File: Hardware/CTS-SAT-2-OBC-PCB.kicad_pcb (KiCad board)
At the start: 6 copper layers, 0 parts

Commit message: Prepare for layout
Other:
- board outline added: 100 x 100 mm
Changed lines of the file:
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@@
 	)
 	(net 0 "")
+	(gr_rect
+		(start 100 50)
+		(end 200 150)
+		(stroke
+			(width 0.05)
+			(type solid)
+		)
+		(fill no)
+		(layer "Edge.Cuts")
+	)
 	(embedded_fonts no)
 )

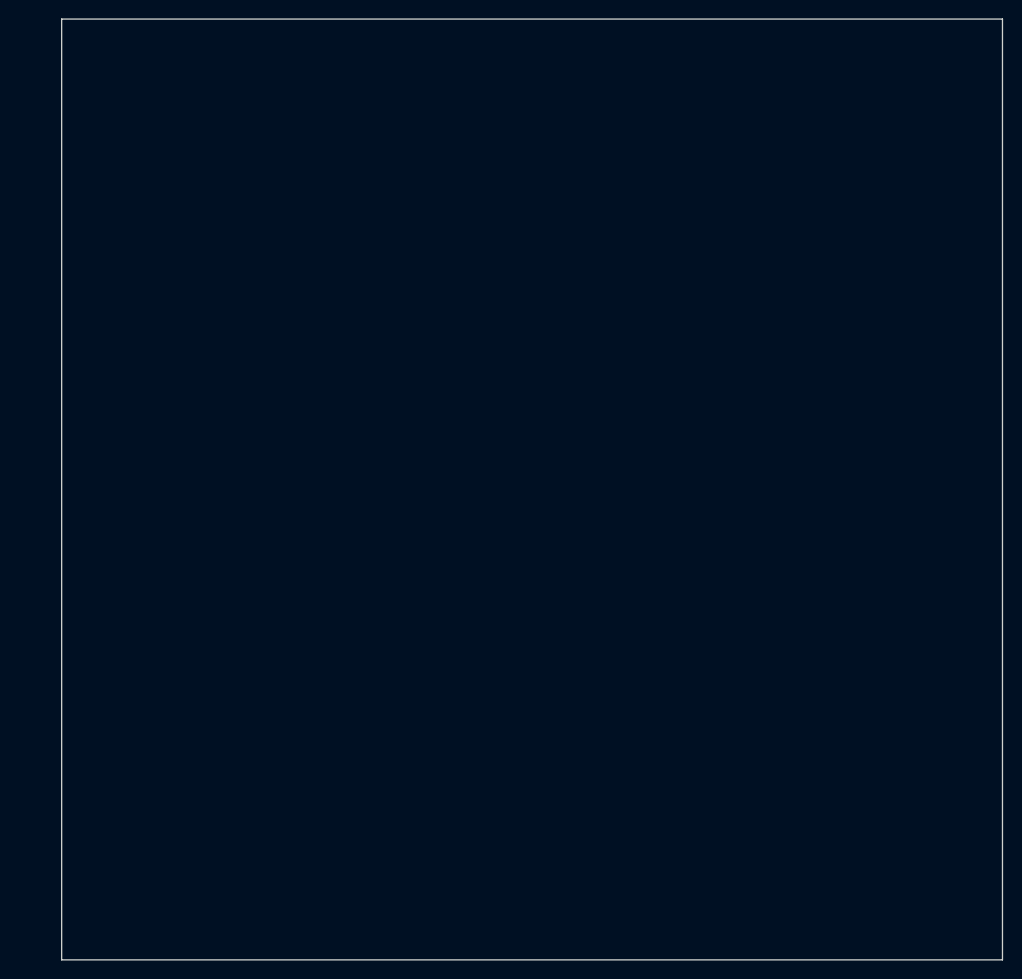
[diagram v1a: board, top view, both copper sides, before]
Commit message: Assign footprints
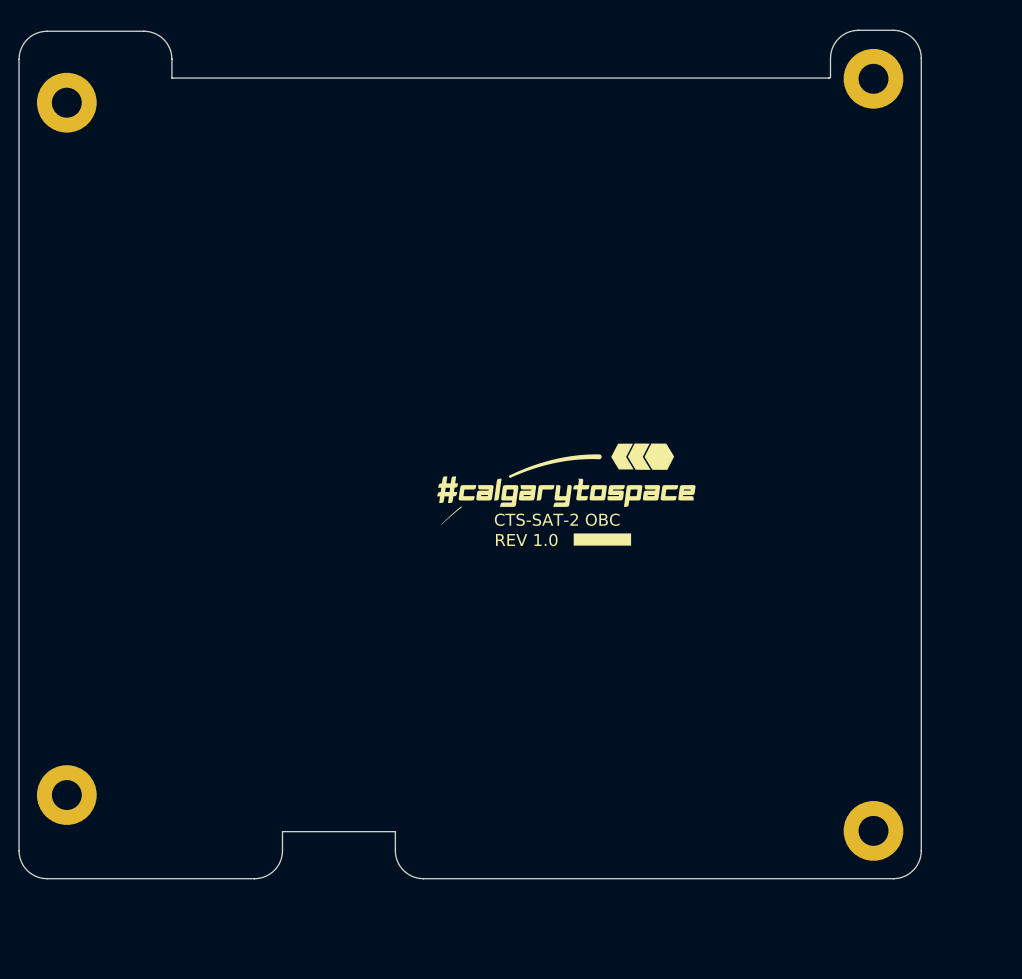
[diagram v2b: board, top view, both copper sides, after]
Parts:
- added *1: PC104 Mounting, OBC Development Board:PC104 MOUNTING POINTS, F.Cu at (102.3, 60.1)
- added *2: PC104 Mounting, OBC Development Board:PC104 MOUNTING POINTS, F.Cu at (186.3, 56.4)
- added *3: PC104 Mounting, OBC Development Board:PC104 MOUNTING POINTS, F.Cu at (102.3, 134.0)
- added *4: PC104 Mounting, OBC Development Board:PC104 MOUNTING POINTS, F.Cu at (184.4, 134.8)
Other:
- board size 100 x 100 mm -> 95.9 x 90.2 mm
- board text added: "CTS-SAT-2 OBC"
- board text added: "REV 1.0"

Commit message: Basic board shape
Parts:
- added C1: 15p, Capacitor_SMD:C_0402_1005Metric, F.Cu at (-55.8, 55.2)
- added C10: 100n, Capacitor_SMD:C_0402_1005Metric, F.Cu at (-52.9, 63.1)
- added C11: 100n, Capacitor_SMD:C_0402_1005Metric, F.Cu at (-50.0, 55.2)
- added C12: 100n, Capacitor_SMD:C_0402_1005Metric, F.Cu at (-50.0, 57.2)
- added C13: 100n, Capacitor_SMD:C_0402_1005Metric, F.Cu at (-50.0, 59.1)
- added C14: 100n, Capacitor_SMD:C_0402_1005Metric, F.Cu at (-50.0, 61.1)
- added C15: 100n, Capacitor_SMD:C_0402_1005Metric, F.Cu at (-81.8, 61.5)
- added C16: 1u, Capacitor_SMD:C_0402_1005Metric, F.Cu at (-81.8, 63.4)
- added C17: 100n, Capacitor_SMD:C_0402_1005Metric, F.Cu at (-81.8, 65.4)
- added C18: 100n, Capacitor_SMD:C_0402_1005Metric, F.Cu at (-81.8, 67.4)
- added C19: 100n, Capacitor_SMD:C_0402_1005Metric, F.Cu at (-81.8, 69.3)
- added C2: 15p, Capacitor_SMD:C_0402_1005Metric, F.Cu at (-55.8, 57.2)
- added C20: 4.7u, Capacitor_SMD:C_0402_1005Metric, F.Cu at (-81.8, 71.3)
- added C21: 100n, Capacitor_SMD:C_0402_1005Metric, F.Cu at (-81.8, 73.3)
- added C22: 100n, Capacitor_SMD:C_0402_1005Metric, F.Cu at (-79.0, 61.5)
- added C23: 100n, Capacitor_SMD:C_0603_1608Metric, F.Cu at (-81.3, 39.1)
- added C24: 100n, Capacitor_SMD:C_0402_1005Metric, F.Cu at (-79.0, 63.4)
- added C25: 100n, Capacitor_SMD:C_0402_1005Metric, F.Cu at (-79.0, 65.4)
- added C26: 100n, Capacitor_SMD:C_0603_1608Metric, F.Cu at (-81.3, 41.6)
- added C27: 100n, Capacitor_SMD:C_0402_1005Metric, F.Cu at (-79.0, 67.4)
- added C28: 100n, Capacitor_SMD:C_0402_1005Metric, F.Cu at (-79.0, 69.3)
- added C29: 15p, Capacitor_SMD:C_0603_1608Metric, F.Cu at (-81.3, 44.1)
- added C3: 100n, Capacitor_SMD:C_0402_1005Metric, F.Cu at (-55.8, 59.1)
- added C30: 100n, Capacitor_SMD:C_0402_1005Metric, F.Cu at (-79.0, 71.3)
- added C31: 100n, Capacitor_SMD:C_0402_1005Metric, F.Cu at (-79.0, 73.3)
- added C32: 100n, Capacitor_SMD:C_0402_1005Metric, F.Cu at (-76.1, 61.5)
- added C33: 100n, Capacitor_SMD:C_0402_1005Metric, F.Cu at (-76.1, 63.4)
- added C34: 100n, Capacitor_SMD:C_0402_1005Metric, F.Cu at (-76.1, 65.4)
- added C35: 100n, Capacitor_SMD:C_0402_1005Metric, F.Cu at (-76.1, 67.4)
- added C36: 4.7uF, Capacitor_SMD:C_1206_3216Metric, F.Cu at (-48.7, 23.4)
- added C37: 4.7uF, Capacitor_SMD:C_1206_3216Metric, F.Cu at (-48.7, 26.8)
- added C38: 4.7uF, Capacitor_SMD:C_1206_3216Metric, F.Cu at (-48.7, 30.1)
- added C39: 0.1u, Capacitor_SMD:C_0603_1608Metric, F.Cu at (-22.0, -14.0)
- added C4: 100n, Capacitor_SMD:C_0402_1005Metric, F.Cu at (-55.8, 61.1)
- added C40: 0.1u, Capacitor_SMD:C_0603_1608Metric, F.Cu at (-22.0, -11.5)
- added C41: 0.1u, Capacitor_SMD:C_0603_1608Metric, F.Cu at (-22.0, -9.01)
- added C42: 0.1u, Capacitor_SMD:C_0603_1608Metric, F.Cu at (-22.0, -6.50)
- added C43: 100pF, Capacitor_SMD:C_0603_1608Metric, F.Cu at (-25.3, 68.1)
- added C44: 100pF, Capacitor_SMD:C_0603_1608Metric, F.Cu at (-25.3, 70.7)
- added C45: 33 pF, Capacitor_SMD:C_0603_1608Metric, F.Cu at (-25.3, 73.2)
- added C46: 33 pF, Capacitor_SMD:C_0603_1608Metric, F.Cu at (-25.3, 75.7)
- added C47: 100pF, Capacitor_SMD:C_0603_1608Metric, F.Cu at (-25.3, 78.2)
- added C48: 0.1uF, Capacitor_SMD:C_0603_1608Metric, F.Cu at (-25.3, 80.7)
- added C49: 0.1uF, Capacitor_SMD:C_0603_1608Metric, F.Cu at (-33.9, 43.5)
- added C5: 100n, Capacitor_SMD:C_0402_1005Metric, F.Cu at (-55.8, 63.1)
- added C50: 1uF, Capacitor_SMD:C_0603_1608Metric, F.Cu at (-33.9, 46.0)
- added C51: 0.1uF, Capacitor_SMD:C_0603_1608Metric, F.Cu at (-33.9, 48.5)
- added C52: 0.1uF, Capacitor_SMD:C_0603_1608Metric, F.Cu at (-33.9, 51.0)
- added C6: 1u, Capacitor_SMD:C_0402_1005Metric, F.Cu at (-52.9, 55.2)
- added C7: 100n, Capacitor_SMD:C_0402_1005Metric, F.Cu at (-52.9, 57.2)
- added C8: 1u, Capacitor_SMD:C_0402_1005Metric, F.Cu at (-52.9, 59.1)
- added C9: 100n, Capacitor_SMD:C_0402_1005Metric, F.Cu at (-52.9, 61.1)
- added D1: LED, CTS-SAT-1:D-SML-D12U1WT86, F.Cu at (-65.9, 68.5)
- added D2: LED, CTS-SAT-1:D-SML-D12U1WT86, F.Cu at (-65.9, 70.6)
- added D3: LED, CTS-SAT-1:D-SML-D12U1WT86, F.Cu at (-65.9, 72.6)
- added D4: LED, CTS-SAT-1:D-SML-D12U1WT86, F.Cu at (-44.1, 22.7)
- added D5: LED, CTS-SAT-1:D-SML-D12U1WT86, F.Cu at (-44.1, 24.8)
- added D6: LED, CTS-SAT-1:D-SML-D12U1WT86, F.Cu at (-44.1, 26.8)
- added IC1: STTS22HTR, STTS22HTR:SON65P200X200X55-7N-D, F.Cu at (-105.5, 68.1)
- added IC2: MT29F1G01ABAFDSF-AAT_F_TR, Package_SO:SOIC-16W_7.5x10.3mm_P1.27mm, F.Cu at (-30.5, -9.24)
- added IC3: MT29F1G01ABAFDSF-AAT_F_TR, Package_SO:SOIC-16W_7.5x10.3mm_P1.27mm, F.Cu at (-30.5, 2.72)
- added IC4: MT29F1G01ABAFDSF-AAT_F_TR, Package_SO:SOIC-16W_7.5x10.3mm_P1.27mm, F.Cu at (-30.5, 14.7)
- added IC5: MT29F1G01ABAFDSF-AAT_F_TR, Package_SO:SOIC-16W_7.5x10.3mm_P1.27mm, F.Cu at (-30.5, 26.6)
- added J10: J-0532610871, CTS-SAT-1:J-532610871, F.Cu at (-72.5, 20.1)
- added J11: J-TSW-106-05-T-S, CTS-SAT-1:J-TSW-106-05-T-S, F.Cu at (-78.4, 0.32)
- added J12: J-0532610671, CTS-SAT-1:J-0532610671, F.Cu at (-88.4, 11.2)
- added J13: J-0532610471, CTS-SAT-1:J-53261-0471, F.Cu at (-101.6, 7.42)
- added J14: J-0532610471, CTS-SAT-1:J-53261-0471, F.Cu at (-101.6, 15.1)
- added J15: J-TSW-106-05-T-S, CTS-SAT-1:J-TSW-106-05-T-S, F.Cu at (-78.4, 4.79)
- added J16: J-0532610671, CTS-SAT-1:J-0532610671, F.Cu at (-88.4, 19.5)
- added J17: J-0532610471, CTS-SAT-1:J-53261-0471, F.Cu at (-101.6, 22.7)
- added J18: 252105, CTS-SAT-1:J-252105, F.Cu at (-31.6, 71.2)
- added J19: 252105, CTS-SAT-1:J-252105, F.Cu at (-31.6, 79.8)
- added J2: 2-Pin Header, Connector_PinHeader_1.27mm:PinHeader_1x02_P1.27mm_Vertical, F.Cu at (-61.9, 23.4)
- added J20: 252105, CTS-SAT-1:J-252105, F.Cu at (-31.6, 88.5)
- added J21: J-0530471010, CTS-SAT-1:J-0530471010, F.Cu at (-9.95, 68.6)
- added J22: J-0530471010, CTS-SAT-1:J-0530471010, F.Cu at (-22.6, 39.6)
- added J23: J-0532610471, CTS-SAT-1:J-53261-0471, F.Cu at (-29.9, 59.3)
- added J24: USB_C_Receptacle_USB2.0_14P, Connector_USB:USB_C_Receptacle_JAE_DX07S024WJ3R400, F.Cu at (-50.2, 41.4)
- added J25: J-0532610471, CTS-SAT-1:J-53261-0471, F.Cu at (-101.6, 30.3)
- added J3: ESQ-126-14-G-D, ESQ-126-14-G-D:SAMTEC_ESQ-126-14-G-D, B.Cu at (112.7, 126.2)
- added J4: ESQ-126-14-G-D, ESQ-126-14-G-D:SAMTEC_ESQ-126-14-G-D, B.Cu at (107.6, 126.2)
- added J5: 2-Pin Header, Connector_PinHeader_1.27mm:PinHeader_1x02_P1.27mm_Vertical, F.Cu at (-57.7, 23.4)
- added J6: 2-Pin Header, Connector_PinHeader_1.27mm:PinHeader_1x02_P1.27mm_Vertical, F.Cu at (-53.6, 23.4)
- added J7: J-0532610671, CTS-SAT-1:J-0532610671, F.Cu at (-88.4, 2.88)
- added J8: J-0532610471, CTS-SAT-1:J-53261-0471, F.Cu at (-101.6, -0.21)
- added J9: J-0532610871, CTS-SAT-1:J-532610871, F.Cu at (-72.5, 11.8)
- added R1: 10k (NP), Resistor_SMD:R_0402_1005Metric, F.Cu at (-59.8, 56.4)
- added R10: 4k7, Resistor_SMD:R_0603_1608Metric, F.Cu at (-59.2, 49.2)
- added R100: 22R, Resistor_SMD:R_0603_1608Metric, F.Cu at (-65.2, 54.2)
- added R101: 22R, Resistor_SMD:R_0603_1608Metric, F.Cu at (-65.2, 56.7)
- added R102: 5k1, Resistor_SMD:R_0603_1608Metric, F.Cu at (-59.2, 51.7)
- added R103: 5k1, Resistor_SMD:R_0603_1608Metric, F.Cu at (-59.2, 54.2)
- added R11: 4k7, Resistor_SMD:R_0603_1608Metric, F.Cu at (-81.3, 46.7)
- added R12: 4k7, Resistor_SMD:R_0603_1608Metric, F.Cu at (-81.3, 49.2)
- added R13: 22R, Resistor_SMD:R_0603_1608Metric, F.Cu at (-81.3, 51.7)
- added R14: 22R, Resistor_SMD:R_0603_1608Metric, F.Cu at (-81.3, 54.2)
- added R15: 0R, Resistor_SMD:R_0603_1608Metric, F.Cu at (-81.3, 56.7)
- added R16: 22R, Resistor_SMD:R_0603_1608Metric, F.Cu at (-81.3, 59.2)
- added R17: 22R, Resistor_SMD:R_0603_1608Metric, F.Cu at (-77.2, 39.1)
- added R18: 0R, Resistor_SMD:R_0603_1608Metric, F.Cu at (-77.2, 41.6)
- added R19: 22R, Resistor_SMD:R_0603_1608Metric, F.Cu at (-77.2, 44.1)
- added R2: 1k, Resistor_SMD:R_0402_1005Metric, F.Cu at (-59.8, 58.4)
- added R20: 22R, Resistor_SMD:R_0603_1608Metric, F.Cu at (-77.2, 46.7)
- added R21: 22R, Resistor_SMD:R_0603_1608Metric, F.Cu at (-77.2, 49.2)
- added R22: 22R, Resistor_SMD:R_0603_1608Metric, F.Cu at (-77.2, 51.7)
- added R23: 22R, Resistor_SMD:R_0603_1608Metric, F.Cu at (-77.2, 54.2)
- added R24: 22R, Resistor_SMD:R_0603_1608Metric, F.Cu at (-77.2, 56.7)
- added R25: 22R, Resistor_SMD:R_0603_1608Metric, F.Cu at (-77.2, 59.2)
- added R26: 22R, Resistor_SMD:R_0603_1608Metric, F.Cu at (-73.2, 39.1)
- added R27: 0R, Resistor_SMD:R_0603_1608Metric, F.Cu at (-73.2, 41.6)
- added R28: 22R, Resistor_SMD:R_0603_1608Metric, F.Cu at (-73.2, 44.1)
- added R29: 22R, Resistor_SMD:R_0603_1608Metric, F.Cu at (-73.2, 46.7)
- added R3: 1k, Resistor_SMD:R_0402_1005Metric, F.Cu at (-59.8, 60.4)
- added R30: 22R, Resistor_SMD:R_0603_1608Metric, F.Cu at (-73.2, 49.2)
- added R31: 22R, Resistor_SMD:R_0603_1608Metric, F.Cu at (-73.2, 51.7)
- added R32: 22R, Resistor_SMD:R_0603_1608Metric, F.Cu at (-73.2, 54.2)
- added R33: 0R, Resistor_SMD:R_0603_1608Metric, F.Cu at (-73.2, 56.7)
- added R34: 0R, Resistor_SMD:R_0603_1608Metric, F.Cu at (-73.2, 59.2)
- added R35: 22R, Resistor_SMD:R_0603_1608Metric, F.Cu at (-69.2, 39.1)
- added R36: 22R, Resistor_SMD:R_0603_1608Metric, F.Cu at (-69.2, 41.6)
- added R37: 22R, Resistor_SMD:R_0603_1608Metric, F.Cu at (-69.2, 44.1)
- added R38: 22R, Resistor_SMD:R_0603_1608Metric, F.Cu at (-69.2, 46.7)
- added R39: 22R, Resistor_SMD:R_0603_1608Metric, F.Cu at (-69.2, 49.2)
- added R4: 0R, Resistor_SMD:R_0603_1608Metric, F.Cu at (-59.2, 39.1)
- added R40: 0R, Resistor_SMD:R_0603_1608Metric, F.Cu at (-69.2, 51.7)
- added R41: 22R, Resistor_SMD:R_0603_1608Metric, F.Cu at (-69.2, 54.2)
- added R42: 4k7, Resistor_SMD:R_0603_1608Metric, F.Cu at (-69.2, 56.7)
- added R43: 4k7, Resistor_SMD:R_0603_1608Metric, F.Cu at (-69.2, 59.2)
- added R44: 4k7, Resistor_SMD:R_0603_1608Metric, F.Cu at (-65.2, 39.1)
- added R45: 4k7, Resistor_SMD:R_0603_1608Metric, F.Cu at (-65.2, 41.6)
- added R46: 4k7, Resistor_SMD:R_0603_1608Metric, F.Cu at (-65.2, 44.1)
- added R47: 4k7, Resistor_SMD:R_0603_1608Metric, F.Cu at (-65.2, 46.7)
- added R48: 1k, Resistor_SMD:R_0603_1608Metric, F.Cu at (-65.2, 49.2)
- added R49: 1k, Resistor_SMD:R_0603_1608Metric, F.Cu at (-65.2, 51.7)
- added R5: 4k7, Resistor_SMD:R_0603_1608Metric, F.Cu at (-59.2, 41.6)
- added R50: 10K, Resistor_SMD:R_0603_1608Metric, F.Cu at (-62.0, 7.92)
- added R51: 10K, Resistor_SMD:R_0603_1608Metric, F.Cu at (-62.0, 10.4)
- added R52: 220R, Resistor_SMD:R_0603_1608Metric, F.Cu at (-62.0, 12.9)
- added R53: 220R, Resistor_SMD:R_0603_1608Metric, F.Cu at (-62.0, 15.4)
- added R54: 10k, Resistor_SMD:R_0603_1608Metric, F.Cu at (-62.0, 18.0)
- added R55: 0R, Resistor_SMD:R_0603_1608Metric, F.Cu at (-62.0, 20.5)
- added R56: 0R, Resistor_SMD:R_0603_1608Metric, F.Cu at (-58.0, 7.92)
- added R57: 0R, Resistor_SMD:R_0603_1608Metric, F.Cu at (-58.0, 10.4)
- added R58: 0R, Resistor_SMD:R_0603_1608Metric, F.Cu at (-58.0, 12.9)
- added R59: 0R, Resistor_SMD:R_0603_1608Metric, F.Cu at (-58.0, 15.4)
- added R6: 27.4, Resistor_SMD:R_0402_1005Metric, F.Cu at (-59.8, 62.4)
- added R60: 4K7, Resistor_SMD:R_0603_1608Metric, F.Cu at (-58.0, 18.0)
- added R61: 22R, Resistor_SMD:R_0603_1608Metric, F.Cu at (-58.0, 20.5)
- added R62: 0R, Resistor_SMD:R_0603_1608Metric, F.Cu at (-53.9, 7.92)
- added R63: 0R, Resistor_SMD:R_0603_1608Metric, F.Cu at (-53.9, 10.4)
- added R64: 0R, Resistor_SMD:R_0603_1608Metric, F.Cu at (-53.9, 12.9)
- added R65: 0R, Resistor_SMD:R_0603_1608Metric, F.Cu at (-53.9, 15.4)
- added R66: 0R, Resistor_SMD:R_0603_1608Metric, F.Cu at (-53.9, 18.0)
- added R67: 4K7, Resistor_SMD:R_0603_1608Metric, F.Cu at (-53.9, 20.5)
- added R68: 0R, Resistor_SMD:R_0603_1608Metric, F.Cu at (-49.9, 7.92)
- added R69: 0R, Resistor_SMD:R_0603_1608Metric, F.Cu at (-49.9, 10.4)
- added R7: 27.4, Resistor_SMD:R_0402_1005Metric, F.Cu at (-59.8, 64.4)
- added R70: 0R, Resistor_SMD:R_0603_1608Metric, F.Cu at (-49.9, 12.9)
- added R71: 4K7, Resistor_SMD:R_0603_1608Metric, F.Cu at (-49.9, 15.4)
- added R72: 10k, Resistor_SMD:R_0603_1608Metric, F.Cu at (-22.0, -3.99)
- added R73: 10k, Resistor_SMD:R_0603_1608Metric, F.Cu at (-22.0, -1.48)
- added R74: 10k, Resistor_SMD:R_0603_1608Metric, F.Cu at (-18.0, -14.0)
- added R75: 10k, Resistor_SMD:R_0603_1608Metric, F.Cu at (-18.0, -11.5)
- added R76: 22R, Resistor_SMD:R_0603_1608Metric, F.Cu at (-18.0, -9.01)
- added R77: 22R, Resistor_SMD:R_0603_1608Metric, F.Cu at (-18.0, -6.50)
- added R78: 22R, Resistor_SMD:R_0603_1608Metric, F.Cu at (-18.0, -3.99)
- added R79: 22R, Resistor_SMD:R_0603_1608Metric, F.Cu at (-18.0, -1.48)
- added R8: 4k7, Resistor_SMD:R_0603_1608Metric, F.Cu at (-59.2, 44.1)
- added R80: 10k, Resistor_SMD:R_0603_1608Metric, F.Cu at (-14.0, -14.0)
- added R81: 10k, Resistor_SMD:R_0603_1608Metric, F.Cu at (-14.0, -11.5)
- added R82: 10k, Resistor_SMD:R_0603_1608Metric, F.Cu at (-14.0, -9.01)
- added R83: 10k, Resistor_SMD:R_0603_1608Metric, F.Cu at (-14.0, -6.50)
- added R84: 100K, Resistor_SMD:R_0603_1608Metric, F.Cu at (-25.3, 83.2)
- added R85: 10K, Resistor_SMD:R_0603_1608Metric, F.Cu at (-25.3, 85.7)
- added R86: 10K, Resistor_SMD:R_0603_1608Metric, F.Cu at (-25.3, 88.2)
- added R87: 0R, Resistor_SMD:R_0603_1608Metric, F.Cu at (-33.9, 53.5)
- added R88: 0R, Resistor_SMD:R_0603_1608Metric, F.Cu at (-33.9, 56.0)
- added R89: 22R, Resistor_SMD:R_0603_1608Metric, F.Cu at (-29.9, 43.5)
- added R9: 4k7, Resistor_SMD:R_0603_1608Metric, F.Cu at (-59.2, 46.7)
- added R90: 22R, Resistor_SMD:R_0603_1608Metric, F.Cu at (-29.9, 46.0)
- added R91: 100K, Resistor_SMD:R_0603_1608Metric, F.Cu at (-29.9, 48.5)
- added R92: 100K, Resistor_SMD:R_0603_1608Metric, F.Cu at (-29.9, 51.0)
- added R93: 100K, Resistor_SMD:R_0603_1608Metric, F.Cu at (-29.9, 53.5)
- added R94: 100K, Resistor_SMD:R_0603_1608Metric, F.Cu at (-29.9, 56.0)
- added R95: 100K, Resistor_SMD:R_0603_1608Metric, F.Cu at (-25.9, 43.5)
- added R96: 100R, Resistor_SMD:R_0603_1608Metric, F.Cu at (-25.9, 46.0)
- added R97: 1K, Resistor_SMD:R_0603_1608Metric, F.Cu at (-25.9, 48.5)
- added R98: 100R, Resistor_SMD:R_0603_1608Metric, F.Cu at (-25.9, 51.0)
- added R99: 1K, Resistor_SMD:R_0603_1608Metric, F.Cu at (-25.9, 53.5)
- added SW1: SW_Push_Dual, PTS526:SMT_FS, F.Cu at (-70.2, 64.0)
- added SW2: SW_Push_Dual, PTS526:SMT_FS, F.Cu at (-43.4, 48.5)
- added U1: W25Q128JVS, W25Q128JVS:SOIC-8_5.23x5.23mm_P1.27mm, F.Cu at (-43.4, 57.6)
- added U2: RP2040, RP2040:RP2040-QFN-56, F.Cu at (154.9, 92.0)
- added U3: STM32L4R5ZITx, Package_QFP:LQFP-144_20x20mm_P0.5mm, F.Cu at (132.4, 95.2)
- added U4: SN74LVC1G14DCKR, CTS-SAT-1:U-SN74LVC1G14DCKR, F.Cu at (-14.9, 72.9)
- added U5: HMC544AE, CTS-SAT-1:U-HMC544AETR, F.Cu at (-20.1, 73.3)
- added U6: U-MAX3378EEUD+T, CTS-SAT-1:U-MAX3378EEUD+T, F.Cu at (-20.5, 57.3)
- added U7: MAX3086EESD+T, CTS-SAT-1:U-MAX3086EESD+T, F.Cu at (-19.3, 47.7)
- added Y1: ABM8-272-T3, Crystal:Crystal_SMD_3225-4Pin_3.2x2.5mm, F.Cu at (-40.5, 40.1)
- added Y2: TG-3541CE_32.7680KXB3, TG-3541CE_32.7680KXB3:TG3541CE327680KXB3, F.Cu at (-71.2, 70.5)
- added Y3: ECS-TXO-2520-33-250-AN-TR, ECS-TXO-2520-33-250-AN-TR:OSC_ECS-TXO-2520-33-250-AN-TR, F.Cu at (-105.0, 64.1)
- moved *4 6.81 mm to (190.8, 132.6)
- moved *1 5.72 mm to (105.1, 55.1)
- moved *2 5.18 mm to (190.8, 58.9)
- moved *3 3.03 mm to (105.1, 135.1)
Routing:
- added copper zone on In1.Cu, net GND
- added copper zone on In4.Cu, net GND
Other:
- outline, holes or cut-outs redrawn
- board text added: "H1"
- board text added: "H2"

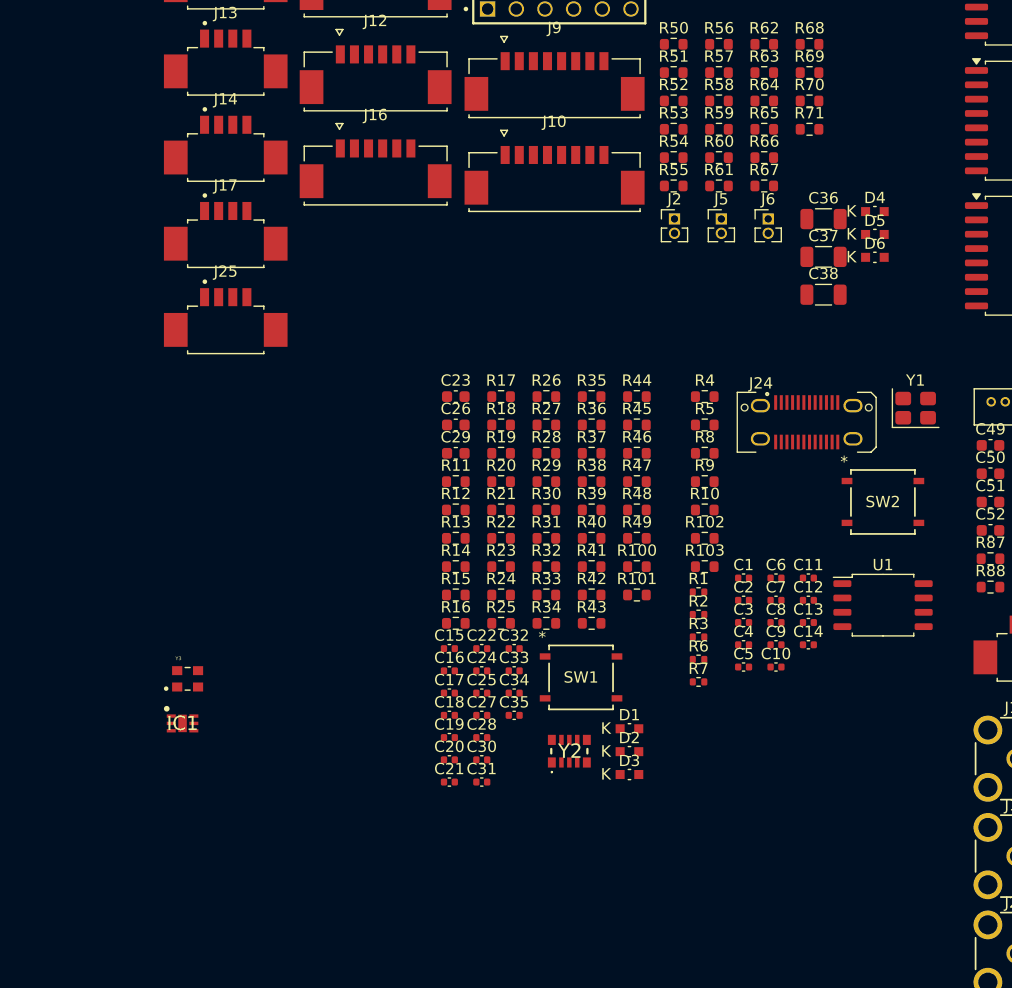
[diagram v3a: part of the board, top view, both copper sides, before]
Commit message: Fix diode footprint assignments
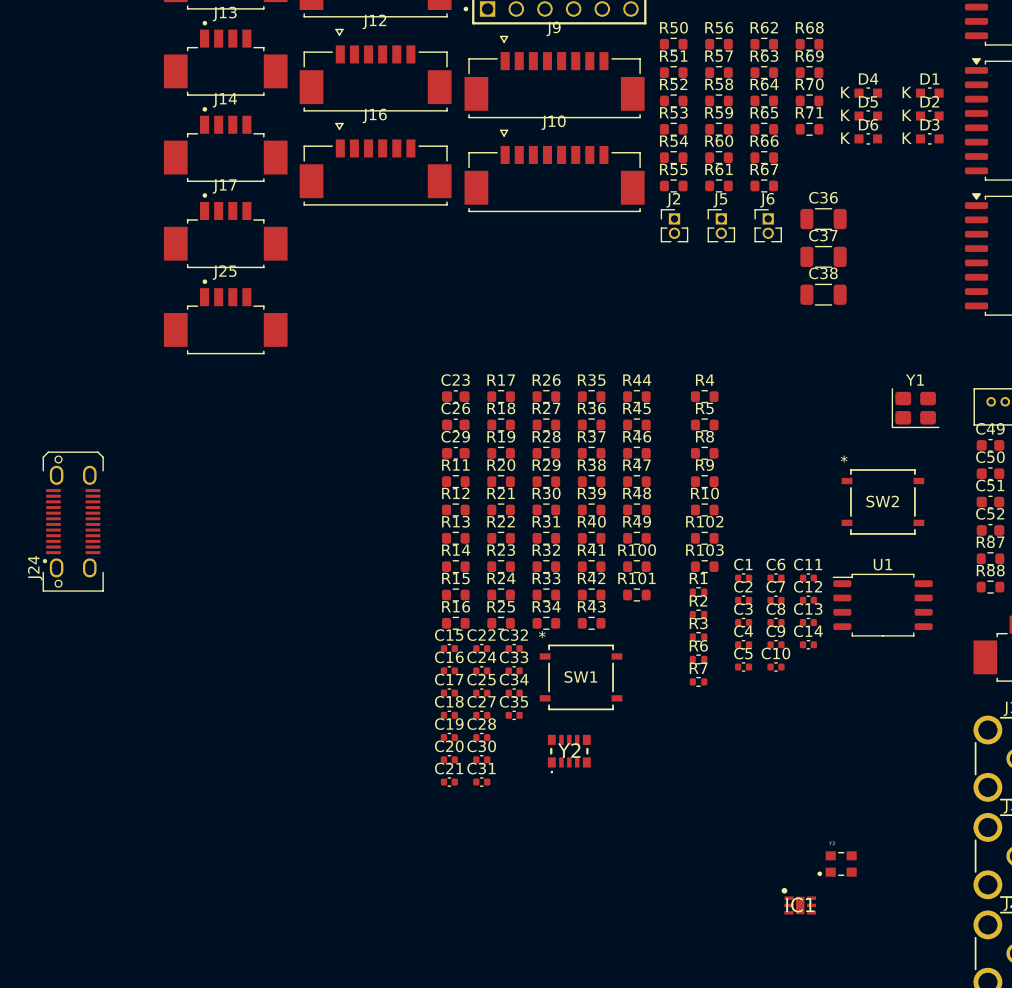
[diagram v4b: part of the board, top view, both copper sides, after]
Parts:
- D1, D2, D3, D4, D5, D6: footprint CTS-SAT-1:D-SML-D12U1WT86 -> CTS-SAT-2:D-SML-D12U1WT86
- moved J24 65.6 mm to (-115.2, 50.2), turned to 90 degrees
- moved D2 62.3 mm to (-39.3, 14.3)
- moved D3 62.3 mm to (-39.3, 16.3)
- moved D1 62.3 mm to (-39.3, 12.2)
- moved Y3 60.2 mm to (-47.1, 80.5)
- moved IC1 57.0 mm to (-50.8, 84.2)
- moved D5 10.5 mm to (-44.7, 14.3)
- moved D6 10.5 mm to (-44.7, 16.3)
- moved D4 10.5 mm to (-44.7, 12.2)

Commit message: Place connectors
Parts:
- J17, J23, J7, J9: moved to B.Cu
- moved J8 317.5 mm to (190.4, 124.5), turned to 90 degrees
- moved J25 303.3 mm to (183.1, 134.9)
- moved J13 299.7 mm to (169.6, 135.0)
- moved J16 294.8 mm to (192.7, 108.7), turned to 90 degrees
- moved J12 292.1 mm to (192.3, 92.0), turned to 90 degrees
- moved J17 281.8 mm to (178.2, 55.8)
- moved J14 271.8 mm to (167.1, 55.5), turned to 180 degrees
- moved J10 270.3 mm to (192.4, 73.3), turned to 90 degrees
- moved J15 230.5 mm to (110.0, 137.5)
- moved J11 229.9 mm to (110.0, 132.1)
- moved J7 226.9 mm to (133.0, 52.9)
- moved J24 200.2 mm to (84.5, 64.8)
- moved J18 197.7 mm to (155.4, 135.4)
- moved J9 193.9 mm to (117.0, 52.8)
- moved J19 184.6 mm to (144.5, 135.3)
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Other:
- board text added: "1&2"
- board text added: "3&4"
- board text added: "ANT1"
- board text added: "ANT2"
- board text added: "Burn Wire"
- board text added: "COMMS"
- board text added: "Camera"
- board text added: "EPS"
- board text added: "GPS"
- board text added: "MPI Power"
- board text added: "Optical Downlink"
- board text added: "RBF"
- board text added: "RP2040 SWD"
- board text added: "STM32 SWD"
- board text added: "Umbilical"

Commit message: Update CTS-SAT-2-OBC-PCB.kicad_pcb
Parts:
- R29, R30: moved to B.Cu
- moved R26 275.2 mm to (187.5, 127.1)
- moved R23 274.0 mm to (187.5, 125.0)
- moved R69 257.8 mm to (187.6, 110.5)
- moved R70 255.9 mm to (187.5, 108.5)
- moved R71 254.3 mm to (187.5, 106.7)
- moved R65 253.6 mm to (187.3, 93.8)
- moved R66 252.2 mm to (187.2, 91.9)
- moved R30 251.7 mm to (178.2, 59.0), turned to 90 degrees
- moved R67 251.0 mm to (187.2, 90.2)
- moved R68 250.5 mm to (187.3, 88.5)
- moved R29 249.8 mm to (176.3, 59.1), turned to 90 degrees
- moved R61 231.2 mm to (170.1, 58.4), turned to 90 degrees
- moved R62 227.3 mm to (167.7, 58.4), turned to 90 degrees
- moved R63 224.8 mm to (165.7, 58.3), turned to 90 degrees
- moved R64 222.4 mm to (163.8, 58.3), turned to 90 degrees
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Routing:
- net GND: track 0.00 -> 44.5 mm, vias 0 -> 15
- net /Connectors/MISO_USART2_RX: track 0.00 -> 2.69 mm
- net Net-(J14-Pad4): track 0.00 -> 2.61 mm
- net Net-(J14-Pad1): track 0.00 -> 2.54 mm
- net /Connectors/MOSI_USART2_TX: track 0.00 -> 2.45 mm
- net /Connectors/MISO_UART5_RX: track 0.00 -> 2.42 mm
- net Net-(J14-Pad3): track 0.00 -> 2.32 mm
- net Net-(J12-Pad4): track 0.00 -> 2.19 mm
- net /Connectors/MOSI_UART5_TX: track 0.00 -> 2.13 mm
- net Net-(J14-Pad2): track 0.00 -> 2.08 mm
- net Net-(J16-Pad4): track 0.00 -> 2.06 mm
- net Net-(J12-Pad6): track 0.00 -> 2.01 mm
- net Net-(J16-Pad5): track 0.00 -> 2.00 mm
- net Net-(J12-Pad5): track 0.00 -> 1.95 mm
- net Net-(J12-Pad2): track 0.00 -> 1.86 mm
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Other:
- board text added: "RP2040 USB"

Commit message: Resistors for connectors
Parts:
- removed R28: 22R, Resistor_SMD:R_0603_1608Metric
- J17, J23, J7, J9, R29, R30: moved to F.Cu
- moved R17 159.2 mm to (170.0, 131.7), turned to -90 degrees
- moved R101 156.6 mm to (183.5, 132.2), turned to -90 degrees
- moved R16 156.1 mm to (167.5, 131.7), turned to -90 degrees
- moved R100 155.6 mm to (182.0, 132.2), turned to -90 degrees
- moved R55 153.5 mm to (186.0, 78.0)
- moved R56 151.6 mm to (187.0, 76.0)
- moved R57 151.1 mm to (187.0, 74.0)
- moved R58 150.5 mm to (187.0, 71.0), turned to 180 degrees
- moved R59 150.2 mm to (187.0, 69.0), turned to 180 degrees
- moved R15 129.8 mm to (136.0, 59.5), turned to 90 degrees
- moved R6 126.9 mm to (151.0, 57.0), turned to -90 degrees
- moved R13 126.7 mm to (134.0, 58.5), turned to 90 degrees
- moved R7 126.3 mm to (149.5, 57.0), turned to -90 degrees
- moved R103 125.6 mm to (153.5, 57.0)
- moved R14 125.4 mm to (132.0, 59.0), turned to 90 degrees
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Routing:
- net GND: track 44.5 -> 94.6 mm, vias 15 -> 25
- net /RP2040/USB_D-: track 0.00 -> 9.63 mm, vias 0 -> 2
- net Net-(J24-CC2): track 0.00 -> 8.38 mm
- net /RP2040/USB_D+: track 0.00 -> 5.61 mm
- net /Connectors/CAM_EN: track 0.00 -> 3.85 mm
- net Net-(J10-Pad1): track 0.00 -> 3.34 mm
- net /Connectors/MISO_UART4_RX: track 0.00 -> 3.02 mm
- net /Connectors/GPS_PPS: track 0.00 -> 2.85 mm
- net Net-(J10-Pad7): track 0.00 -> 2.73 mm
- net Net-(J24-CC1): track 0.00 -> 2.57 mm
- net /Connectors/BOOM_CTRL_2: track 0.00 -> 2.55 mm
- net /Connectors/BOOM_CTRL_1: track 0.00 -> 2.55 mm
- net Net-(J10-Pad3): track 0.00 -> 2.55 mm
- net /Connectors/MOSI_UART4_TX: track 0.00 -> 2.54 mm
- net Net-(J10-Pad6): track 0.00 -> 2.42 mm
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
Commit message: make most changes from design review
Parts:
- added R104: 22R, Resistor_SMD:R_0603_1608Metric, F.Cu at (31.2, 23.4)
- added R105: 0R, Resistor_SMD:R_0603_1608Metric, F.Cu at (31.2, 25.9)
- added R106: 0R, Resistor_SMD:R_0603_1608Metric, F.Cu at (31.2, 28.5)
- added R107: 0R, Resistor_SMD:R_0603_1608Metric, F.Cu at (31.2, 31.0)
- added R108: 22R, Resistor_SMD:R_0603_1608Metric, F.Cu at (31.2, 33.5)
- added R109: 22R, Resistor_SMD:R_0603_1608Metric, F.Cu at (35.2, 23.4)
- added R110: 22R, Resistor_SMD:R_0603_1608Metric, F.Cu at (35.2, 25.9)
- added R111: 22R, Resistor_SMD:R_0603_1608Metric, F.Cu at (35.2, 28.5)
- added R112: 22R, Resistor_SMD:R_0603_1608Metric, F.Cu at (35.2, 31.0)
- added R113: 22R, Resistor_SMD:R_0603_1608Metric, F.Cu at (35.2, 33.5)
- added R20: 0R, Resistor_SMD:R_0603_1608Metric, F.Cu at (25.2, 23.4)
- added R22: 0R, Resistor_SMD:R_0603_1608Metric, F.Cu at (25.2, 25.9)
- added R26: 0R, Resistor_SMD:R_0603_1608Metric, F.Cu at (25.2, 28.5)
- added R28: 22R, Resistor_SMD:R_0603_1608Metric, F.Cu at (25.2, 31.0)
- added R30: 0R, Resistor_SMD:R_0603_1608Metric, F.Cu at (25.2, 33.5)
- added R34: 22R, Resistor_SMD:R_0603_1608Metric, F.Cu at (25.2, 36.0)
- added R36: 0R, Resistor_SMD:R_0603_1608Metric, F.Cu at (25.2, 38.5)
- C19: value 100n -> 4.7u
- C20: value 4.7u -> 100n
- R14: value 22R -> 0R
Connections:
- R2 pad 1: Net-(U1-~{CS}) -> Net-(U2-QSPI_SS)
- R4 pad 1: /Antenna/UHF_CTRL -> Net-(U2-GPIO4)
- R4 pad 2: Net-(U2-GPIO4) -> /Antenna/UHF_CTRL
- R89 pad 1: /MPI/MOSI_MPI_TX_EN -> Net-(U6-IO_VL3)
- R89 pad 2: Net-(U6-IO_VL3) -> /MPI/MOSI_MPI_TX_EN
- SW1 pad 3: Net-(R48-Pad2) -> (no net)
- SW1 pad 4: GND -> (no net)
- SW2 pad 3: /RP2040/~{BOOTSEL} -> (no net)
- SW2 pad 4: GND -> (no net)
- U1 pad 6: Net-(U1-CLK) -> /RP2040/RP2040_MEM_SCLK
- U2 pad 12: /RP2040/SPI1_CS0 -> Net-(U2-GPIO9)
- U2 pad 13: /RP2040/SPI1_SCK -> Net-(U2-GPIO10)
- U2 pad 14: /RP2040/SPI1_TX -> Net-(U2-GPIO11)
- U2 pad 15: /RP2040/SPI1_RX -> Net-(U2-GPIO12)
- U2 pad 51: Net-(U1-IO3) -> Net-(U2-QSPI_SD3)
- U2 pad 52: Net-(U1-CLK) -> Net-(U2-QSPI_SCLK)
- U2 pad 53: Net-(U1-DI(IO0)) -> Net-(U2-QSPI_SD0)
- U2 pad 54: Net-(U1-IO2) -> Net-(U2-QSPI_SD2)
- U2 pad 55: Net-(U1-DO(IO1)) -> Net-(U2-QSPI_SD1)
- U2 pad 56: Net-(U1-~{CS}) -> Net-(U2-QSPI_SS)
